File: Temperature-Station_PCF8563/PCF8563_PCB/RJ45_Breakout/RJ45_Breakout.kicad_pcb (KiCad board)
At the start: 2 copper layers, 31 parts, among them J1 MHRJJ66NFRA, J2 MHRJJ66NFRA, J3 MHRJJ66NFRA, J4 MHRJJ66NFRA, J5 MHRJJ66NFRA, J6 MHRJJ66NFRA, J7 MHRJJ66NFRA, J8 MHRJJ66NFRA, J9 Flex, U1 LM1117-3.3

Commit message: Updated boards and sketches
Boards:
Sandwich-like layout so you can connect directly do DHT sensors or use i2c expansion (8 slots).
Boards support 1wire, DHT11/21/22 sensors and require custom wiring.
Reduced size of boards

Sketch:
Hermetized settings (no way to read passwords)
Used settingsHandler to hold every field that will have to be saved
Fixed AP launch in PCF8563
Rolled back Pinger library due to readability issues.
WIP: Use external memory only for emergency sensor file and permanently for readings
TESTING: Update via curl
TESTING: Set time and date via webpage
WIP: Change settings via webpage
WIP: Change login credentials via webpage
Documentation: coming soon
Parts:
- moved D2 34.4 mm to (146.7, 83.8)
- moved C1 19.6 mm to (119.9, 83.2), turned to 180 degrees
- moved F1 17.5 mm to (119.9, 86.4)
- moved U1 17.3 mm to (137.2, 83.8)
- moved D1 12.0 mm to (128.9, 83.8)
- moved J9 10.8 mm to (81.3, 81.3)
- moved C2 10.2 mm to (113.5, 85.1), turned to 180 degrees
- moved R1 1.27 mm to (91.6, 100.3)
- moved R10 1.27 mm to (100.5, 100.3)
- moved R11 1.27 mm to (115.7, 100.3)
- moved R12 1.27 mm to (131.0, 100.3)
- moved R13 1.27 mm to (146.2, 100.3)
- moved R14 1.27 mm to (161.4, 100.3)
- moved R15 1.27 mm to (176.7, 100.3)
- moved R16 1.27 mm to (191.9, 100.3)
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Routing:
- net dht_4: track 84.7 -> 73.9 mm
- net dht_7: track 122.8 -> 112.0 mm
- net dht_6: track 110.1 -> 99.3 mm
- net dht_5: track 97.4 -> 86.6 mm
- net dht_3: track 72.0 -> 61.2 mm
- net dht_2: track 59.3 -> 48.5 mm
- net dht_1: track 46.6 -> 35.8 mm
- net dht_0: track 33.9 -> 23.1 mm
- net 1wire: track 172.7 -> 161.9 mm
- net Vin: track 32.2 -> 27.1 mm
- net Net-(D1-Pad2): track 29.8 -> 24.8 mm
- net 3V3: track 251.6 -> 249.0 mm
- net Net-(J8-Pad5): track 5.34 -> 4.07 mm
- net Net-(J7-Pad5): track 5.34 -> 4.07 mm
- net Net-(J6-Pad5): track 5.34 -> 4.07 mm
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
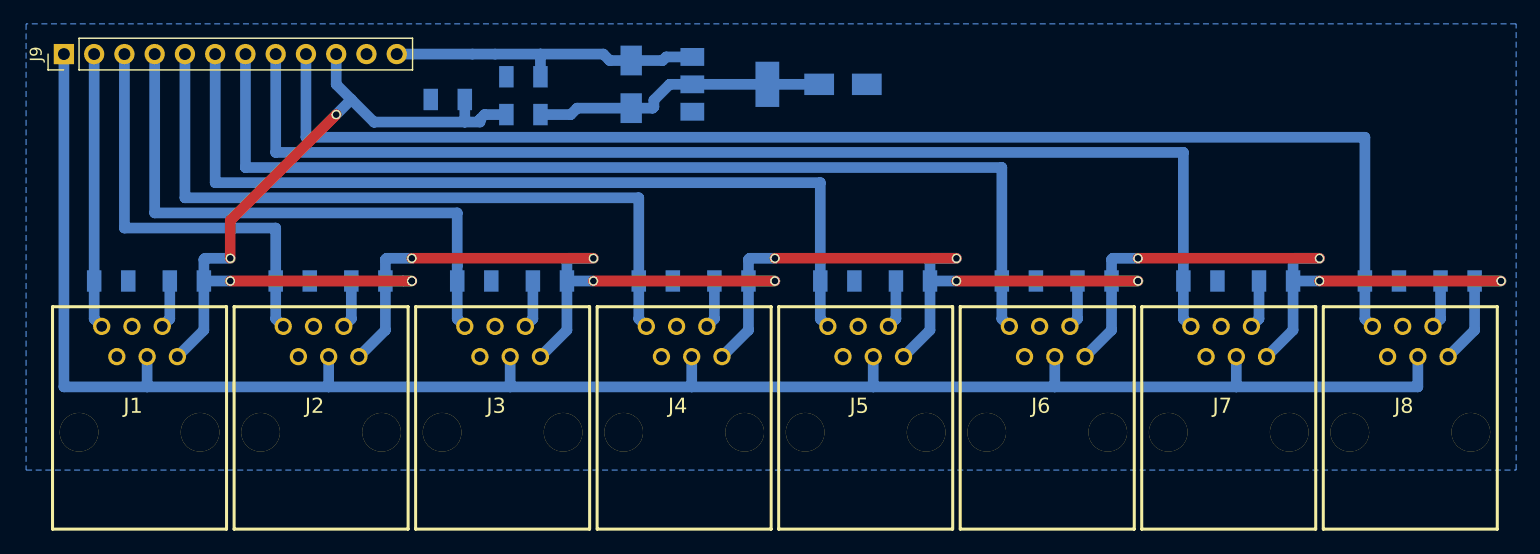
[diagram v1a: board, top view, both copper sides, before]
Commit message: Muxtemp update
Fixed begin()
Removed function that only read ports (now it will only probe&read)
Fixed typo (requesting fixed number of devices even if real amount is different)
TODO: 1wire connection
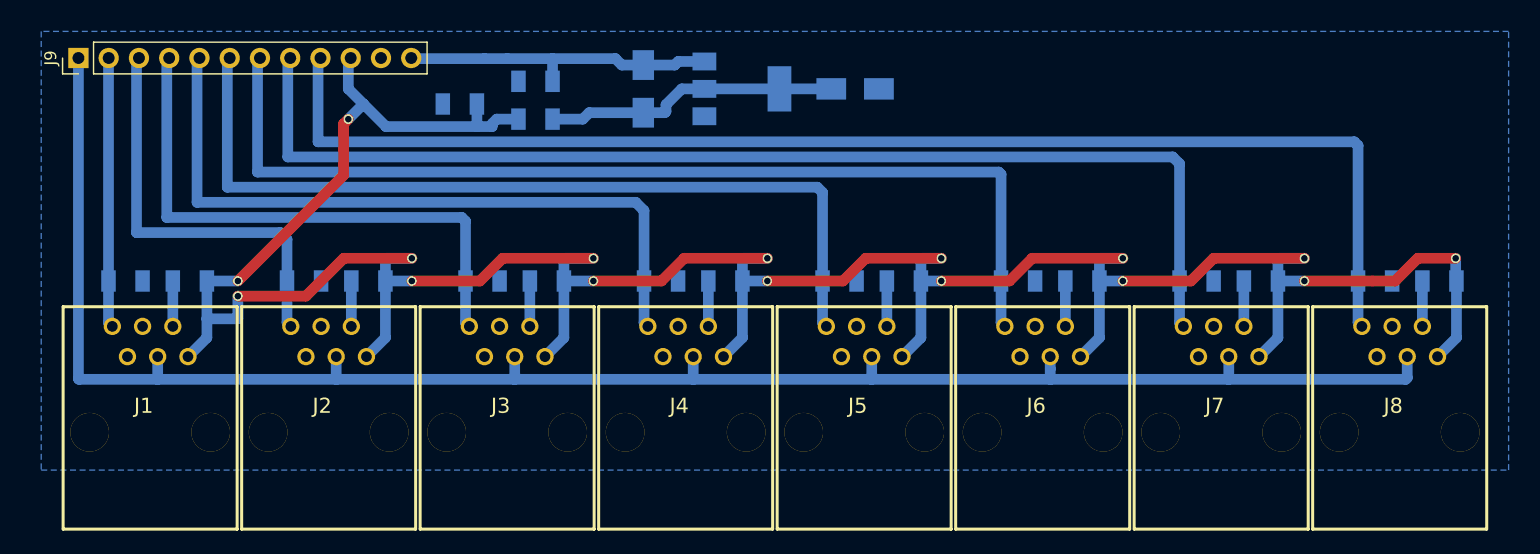
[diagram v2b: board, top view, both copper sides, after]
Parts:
- moved R8 1.52 mm to (196.8, 100.3)
- moved R7 1.27 mm to (181.8, 100.3)
- moved J9 1.26 mm to (82.5, 81.6)
- moved R9 1.20 mm to (86.5, 100.3)
- moved C2 1.09 mm to (114.5, 85.5)
- moved C1 1.09 mm to (120.9, 83.6)
- moved D1 1.09 mm to (129.9, 84.2)
- moved D2 1.09 mm to (147.7, 84.2)
- moved F1 1.09 mm to (120.9, 86.7)
- moved U1 1.09 mm to (138.2, 84.2)
- moved R6 1.02 mm to (166.8, 100.3)
- moved R10 0.95 mm to (101.4, 100.3)
- moved J1 0.89 mm to (88.5, 104.1)
- moved J8 0.89 mm to (193.4, 104.1)
- moved R5 0.76 mm to (151.8, 100.3)
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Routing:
- net 1wire: track 161.9 -> 153.7 mm
- net dht_7: track 112.0 -> 109.7 mm
- net dht_6: track 99.3 -> 97.1 mm
- net dht_5: track 86.6 -> 84.9 mm
- net dht_4: track 73.9 -> 72.3 mm
- net dht_3: track 61.2 -> 59.7 mm
- net dht_2: track 48.5 -> 47.5 mm
- net dht_1: track 35.8 -> 34.9 mm
- net 3V3: track 249.0 -> 249.5 mm, vias 17 -> 16

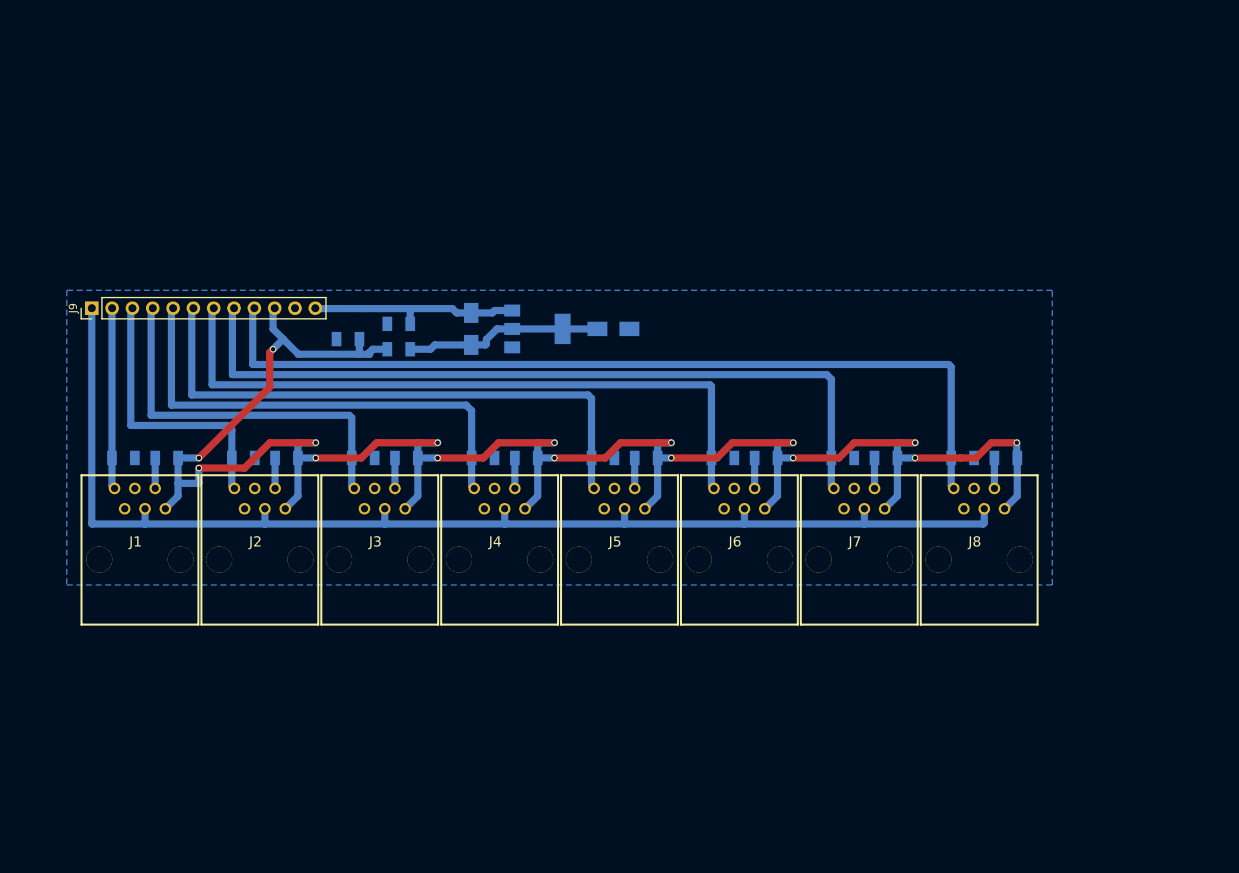
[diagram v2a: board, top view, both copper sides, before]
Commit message: Cleaned boards up
Merged RJ45_I2C with RJ45_Breakout into one schematic
Added fully-integrated Muxtemp board
Started working on Mainboard+Muxtemp board

Settings page (html) is now functional. Backend WIP.

SettingsHandler(PCF8563) is now cleaned up a bit, added optional define to include debug interface
Added option to configure OTA updater as well as WebUpdater
SettingsHandler(Slave): see above
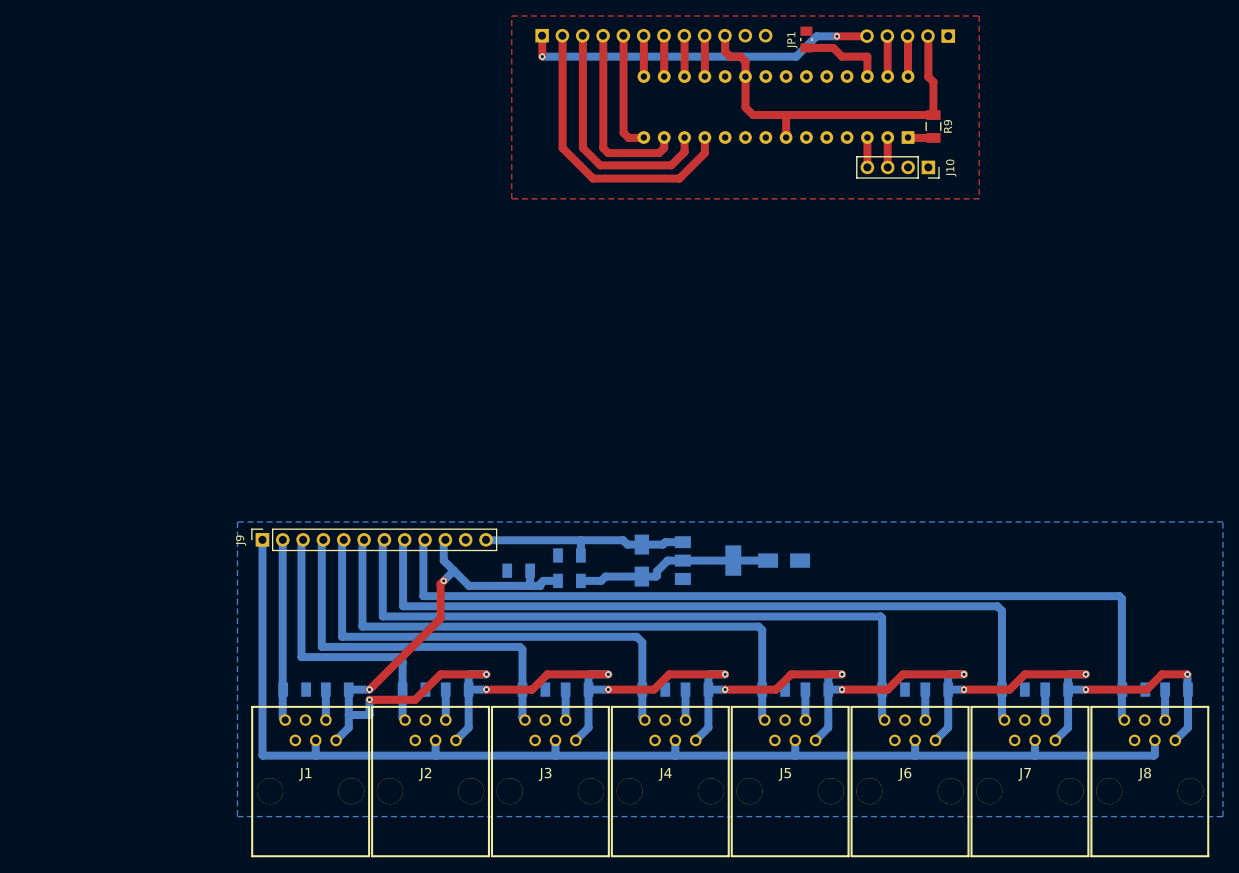
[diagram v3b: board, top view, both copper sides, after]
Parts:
- added J10: Prog, Connector_PinSocket_2.54mm:PinSocket_1x04_P2.54mm_Vertical, F.Cu at (187.1, 64.0)
- added J11: Out, Connector_PinHeader_2.54mm:PinHeader_1x05_P2.54mm_Horizontal, B.Cu at (189.6, 47.6)
- added J12: Flex, Connector_PinHeader_2.54mm:PinHeader_1x12_P2.54mm_Vertical, B.Cu at (138.8, 47.5)
- added JP1: bypass1Wire, Resistor_SMD:R_0805_2012Metric_Pad1.15x1.50mm_HandSolder, F.Cu at (171.8, 48.0)
- added R17: 33k, Resistor_SMD:R_1206_3216Metric, B.Cu at (212.8, 129.3)
- added U2: ATmega328-PU, Package_DIP:DIP-28_W7.62mm, B.Cu at (184.5, 60.3)
- J9: value Flex -> Conn_01x12; footprint Connector_PinHeader_2.54mm:PinHeader_1x12_P2.54mm_Vertical -> Connector_PinSocket_2.54mm:PinSocket_1x12_P2.54mm_Vertical
- R9: value 33k -> 10k; moved to F.Cu
- moved R9 109.4 mm to (187.7, 58.9), turned to 270 degrees
- moved D1 36.0 mm to (151.3, 113.2)
- moved D2 36.0 mm to (169.0, 113.2)
- moved J5 36.0 mm to (169.8, 133.1)
- moved J8 36.0 mm to (214.8, 133.1)
- moved R3 36.0 mm to (143.2, 129.3)
- moved R6 36.0 mm to (188.1, 129.3)
- moved R8 36.0 mm to (218.1, 129.3)
- moved U1 36.0 mm to (159.5, 113.2)
- moved C1 36.0 mm to (142.2, 112.5)
- moved C2 36.0 mm to (135.9, 114.4)
- moved F1 36.0 mm to (142.2, 115.7)
- moved J1 36.0 mm to (109.9, 133.1)
- moved J2 36.0 mm to (124.8, 133.1)
- moved J3 36.0 mm to (139.8, 133.1)
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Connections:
- R10 pad 2: dht_1 -> dht_0
- R11 pad 2: dht_2 -> dht_1
- R12 pad 2: dht_3 -> dht_2
- R13 pad 2: dht_4 -> dht_3
- R14 pad 2: dht_5 -> dht_4
- R15 pad 2: dht_6 -> dht_5
- R16 pad 2: dht_7 -> dht_6
- R9 pad 1: GND -> 3V3
- R9 pad 2: dht_0 -> Net-(J10-Pad2)
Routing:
- net 3V3: track 249.5 -> 297.0 mm
- net 1wire: track 153.7 -> 197.9 mm, vias 0 -> 2
- net dht_0: track 22.7 -> 59.2 mm
- net dht_1: track 34.9 -> 64.9 mm
- net dht_2: track 47.5 -> 70.9 mm
- net dht_3: track 59.7 -> 74.6 mm
- net Net-(JP1-Pad1): track 0.00 -> 10.6 mm
- net dht_7: track 109.7 -> 114.8 mm
- net dht_5: track 84.9 -> 90.0 mm
- net SDA: track 0.00 -> 5.08 mm
- net SCL: track 0.00 -> 5.08 mm
- net dht_6: track 97.1 -> 102.2 mm
- net dht_4: track 72.3 -> 77.4 mm
- net Net-(J10-Pad4): track 0.00 -> 3.73 mm
- net Net-(J10-Pad3): track 0.00 -> 3.73 mm
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- added copper zone on F.Cu, net GND
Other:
- net class Default: trace_width 0.9 -> 1; via_drill 0.55 -> 0.4
